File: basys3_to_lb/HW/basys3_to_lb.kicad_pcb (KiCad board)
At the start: 2 copper layers, 47.2 x 69.1 mm, 35 parts, among them J1 USB_C_Receptacle_USB2.0, J10 Conn_01x02, J11 Conn_02x02_Odd_Even, J12 Conn_02x02_Odd_Even, J13 Conn_02x02_Odd_Even, J2 Conn_02x22_Odd_Even, J3 Conn_01x02, J4 Conn_02x05_Odd_Even, J5 Conn_01x03, J6 Conn_01x03, J7 Conn_01x03, J8 Conn_01x05, J9 Conn_01x03, SW1 SW_Push, U1 MT9700, U2 CH552G

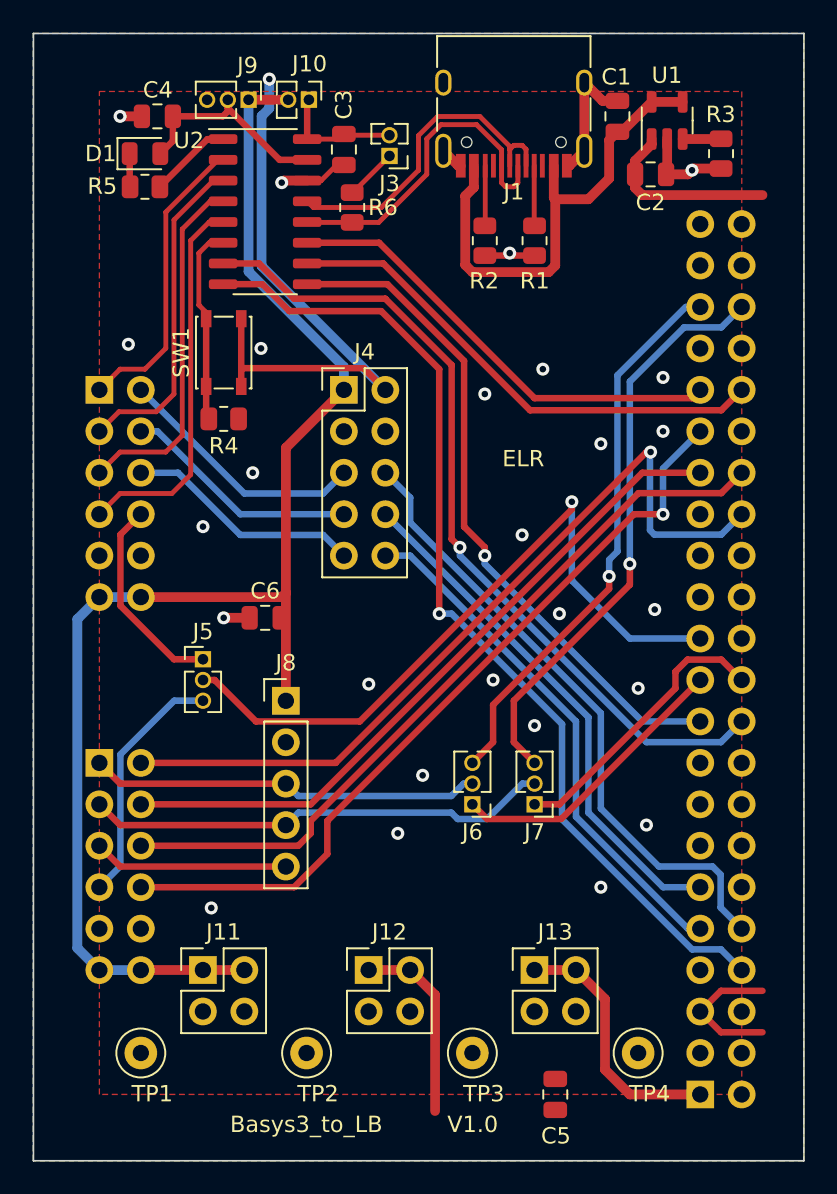
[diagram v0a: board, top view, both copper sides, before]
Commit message: Fixed wrong voltage for reset switch in basys3_to_lb
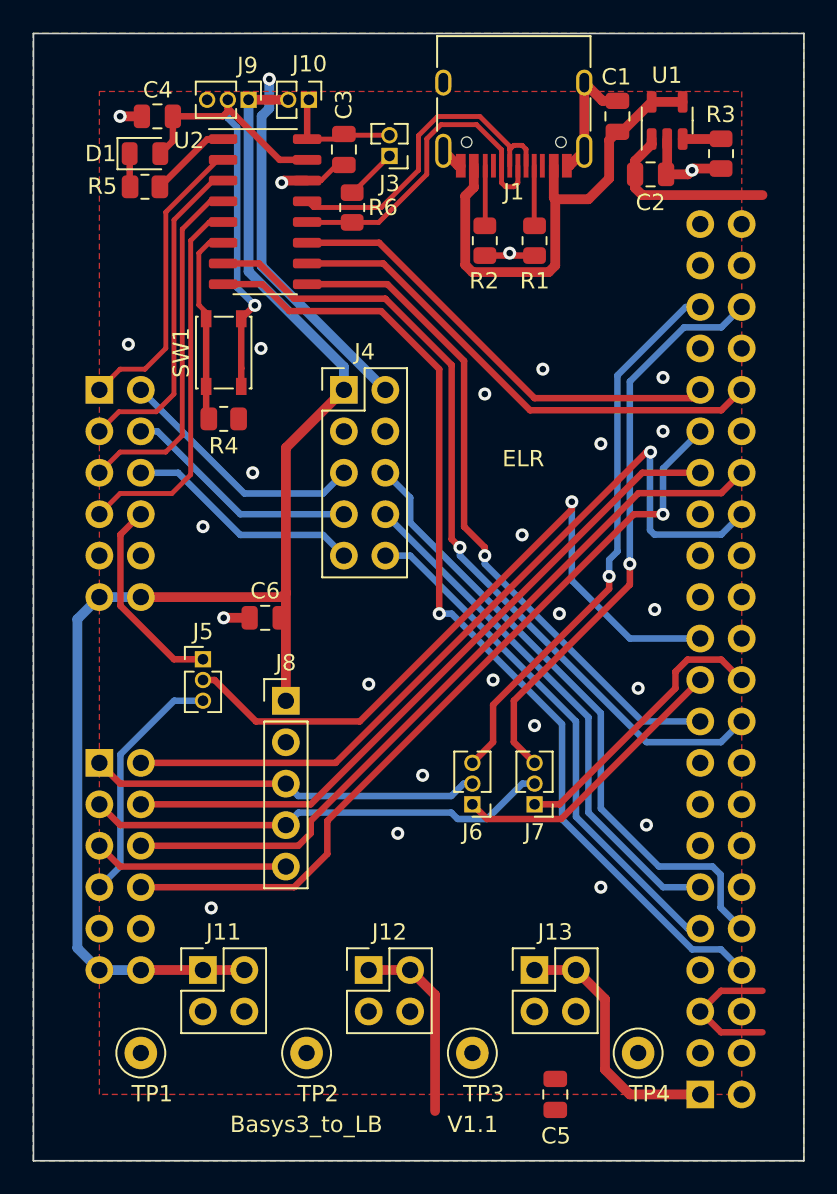
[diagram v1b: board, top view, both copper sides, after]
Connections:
- SW1 pad 2: +5V -> /MCU_VDD
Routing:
- net /MCU_VDD: track 13.5 -> 32.1 mm, vias 0 -> 1
- net +5V: track 67.8 -> 54.3 mm
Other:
- board text added: "V1.1"
- board text removed: "V1.0"
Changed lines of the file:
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@@
       (net 49 "/RST") (pinfunction "1") (pintype "passive"))
     (pad "2" smd rect (at 2.075 1.075 90) (size 1.05 0.65) (layers "F.Cu" "F.Paste" "F.Mask")
-      (net 3 "+5V") (pinfunction "2") (pintype "passive"))
+      (net 66 "/MCU_VDD") (pinfunction "2") (pintype "passive"))
     (pad "2" smd rect (at -2.075 1.075 90) (size 1.05 0.65) (layers "F.Cu" "F.Paste" "F.Mask")
-      (net 3 "+5V") (pinfunction "2") (pintype "passive"))
+      (net 66 "/MCU_VDD") (pinfunction "2") (pintype "passive"))
     (model "${KICAD6_3DMODEL_DIR}/Button_Switch_SMD.3dshapes/SW_SPST_PTS810.wrl"
       (offset (xyz 0 0 0))
@@
   )
   (gr_rect locked (start 117.88 59.436) (end 165.1 128.524) (layer "Edge.Cuts") (width 0.1) (fill none))
-  (gr_text "V1.0" (at 144.8 126.3) (layer "F.SilkS")
+  (gr_text "V1.1" (at 144.8 126.3) (layer "F.SilkS")
     (effects (font (size 1 1) (thickness 0.15)))
   )
@@
   (segment (start 154.752 67.244) (end 154.752 68.072) (width 0.6) (layer "F.Cu") (net 3))
   (segment (start 155.768 65.9075) (end 155.768 66.228) (width 0.6) (layer "F.Cu") (net 3))
-  (segment (start 130.615 81.069) (end 130.615 79.951) (width 0.4) (layer "F.Cu") (net 3))
   (segment (start 140.965 116.835) (end 142.494 118.364) (width 0.6) (layer "F.Cu") (net 3))
   (segment (start 155.768 66.228) (end 154.752 67.244) (width 0.6) (layer "F.Cu") (net 3))
@@
   (segment (start 154.752 68.072) (end 154.752 68.9) (width 0.6) (layer "F.Cu") (net 3))
   (segment (start 158.745 119.38) (end 160.015 120.65) (width 0.4) (layer "F.Cu") (net 3))
-  (segment (start 130.615 79.951) (end 130.615 76.919) (width 0.4) (layer "F.Cu") (net 3))
-  (segment (start 139.446 81.28) (end 138.117 79.951) (width 0.4) (layer "F.Cu") (net 3))
   (segment (start 160.015 118.11) (end 162.56 118.11) (width 0.4) (layer "F.Cu") (net 3))
   (segment (start 154.752 68.9) (end 155.194 69.342) (width 0.6) (layer "F.Cu") (net 3))
   (segment (start 155.194 69.342) (end 162.56 69.342) (width 0.6) (layer "F.Cu") (net 3))
   (segment (start 138.425 116.835) (end 140.965 116.835) (width 0.6) (layer "F.Cu") (net 3))
-  (segment (start 138.117 79.951) (end 130.615 79.951) (width 0.4) (layer "F.Cu") (net 3))
   (via (at 132.334 62.23) (size 0.8) (drill 0.4) (layers "F.Cu" "B.Cu") (net 3))
   (segment (start 131.86352 73.69752) (end 131.86352 64.499511) (width 0.6) (layer "B.Cu") (net 3))
@@
   (segment (start 134.655 65.913) (end 134.655 63.607) (width 0.4) (layer "F.Cu") (net 65))
   (segment (start 129.794 64.207106) (end 129.485106 64.516) (width 0.4) (layer "F.Cu") (net 66))
+  (segment (start 131.434 76.1) (end 130.615 76.919) (width 0.4) (layer "F.Cu") (net 66))
   (segment (start 125.6515 66.802) (end 126.426 66.0275) (width 0.4) (layer "F.Cu") (net 66))
+  (segment (start 131.45 76.1) (end 131.434 76.1) (width 0.4) (layer "F.Cu") (net 66))
+  (segment (start 130.615 81.069) (end 130.615 79.951) (width 0.4) (layer "F.Cu") (net 66))
   (segment (start 132.969 67.183) (end 129.794 64.008) (width 0.4) (layer "F.Cu") (net 66))
   (segment (start 126.426 66.0275) (end 126.426 64.516) (width 0.4) (layer "F.Cu") (net 66))
   (segment (start 129.794 64.008) (end 129.794 63.5) (width 0.4) (layer "F.Cu") (net 66))
+  (segment (start 130.615 79.951) (end 130.615 76.919) (width 0.4) (layer "F.Cu") (net 66))
   (segment (start 129.794 63.5) (end 129.794 64.207106) (width 0.4) (layer "F.Cu") (net 66))
   (segment (start 129.485106 64.516) (end 126.426 64.516) (width 0.4) (layer "F.Cu") (net 66))
   (segment (start 134.655 67.183) (end 132.969 67.183) (width 0.4) (layer "F.Cu") (net 66))
+  (via (at 131.45 76.1) (size 0.8) (drill 0.4) (layers "F.Cu" "B.Cu") (net 66))
+  (segment (start 129.794 64.62952) (end 129.794 63.5) (width 0.4) (layer "B.Cu") (net 66))
+  (segment (start 131.45 76.1) (end 130.36448 75.01448) (width 0.4) (layer "B.Cu") (net 66))
+  (segment (start 130.36448 65.2) (end 129.794 64.62952) (width 0.4) (layer "B.Cu") (net 66))
+  (segment (start 130.36448 75.01448) (end 130.36448 65.2) (width 0.4) (layer "B.Cu") (net 66))
   (segment (start 137.414 69.1915) (end 137.4525 69.1915) (width 0.3) (layer "F.Cu") (net 67))
   (segment (start 137.4525 69.1915) (end 139.7 66.944) (width 0.3) (layer "F.Cu") (net 67))
   (zone (net 2) (net_name "GND") (layer "F.Cu") (hatch edge 0.508)
     (priority 1)
-    (connect_pads (clearance 0.3))
+    (connect_pads thru_hole_only (clearance 0.3))
     (min_thickness 0.254) (filled_areas_thickness no)
     (fill yes (thermal_gap 0.508) (thermal_bridge_width 0.508))
@@
   )
   (zone (net 3) (net_name "+5V") (layer "F.Cu") (hatch edge 0.508)
-    (connect_pads (clearance 0.3))
+    (connect_pads thru_hole_only (clearance 0.3))
     (min_thickness 0.254) (filled_areas_thickness no)
     (fill yes (thermal_gap 0.508) (thermal_bridge_width 0.508))
@@
   )
   (zone (net 2) (net_name "GND") (layer "B.Cu") (hatch edge 0.508)
-    (connect_pads (clearance 0.3))
+    (connect_pads thru_hole_only (clearance 0.3))
     (min_thickness 0.254) (filled_areas_thickness no)
     (fill yes (thermal_gap 0.508) (thermal_bridge_width 0.508))
